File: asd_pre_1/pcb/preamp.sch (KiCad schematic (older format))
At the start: 0 parts

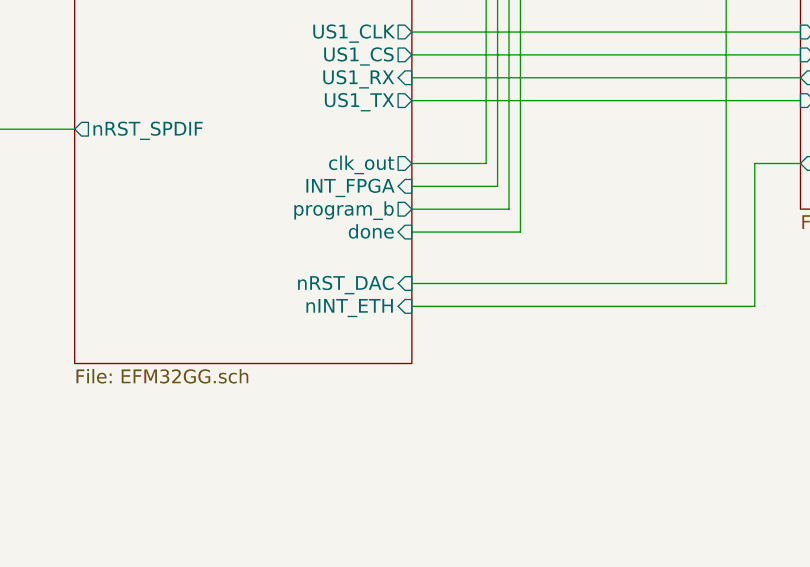
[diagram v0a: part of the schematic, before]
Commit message: Updated schematics and PCB.  Removed some minor errors with the first prototype.
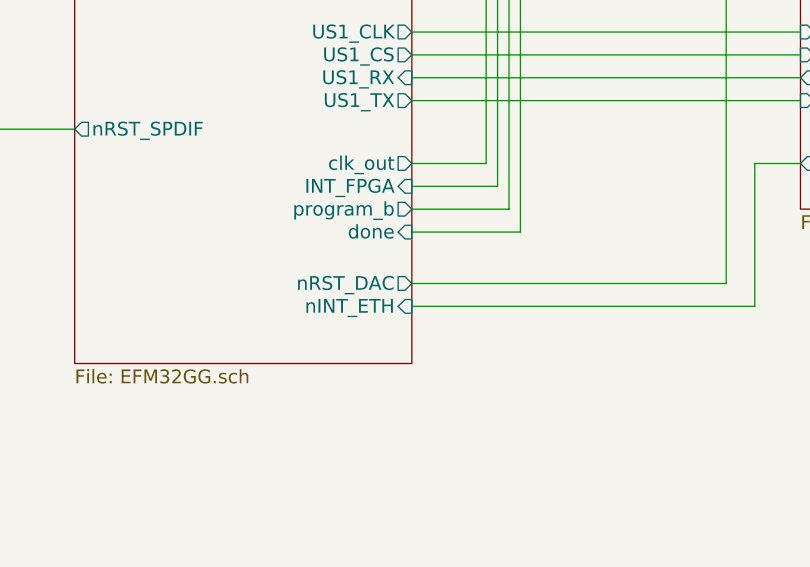
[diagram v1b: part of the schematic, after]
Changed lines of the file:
@@
 EESchema Schematic File Version 2
+LIBS:preamp-rescue
 LIBS:power
 LIBS:device
@@
 LIBS:memory
 LIBS:xilinx
-LIBS:special
 LIBS:microcontrollers
 LIBS:dsp
@@
 encoding utf-8
 Sheet 1 9
-Title ""
+Title "AsD Pre 1 Digital Preamplifier"
 Date ""
 Rev ""
-Comp ""
+Comp "Asbjørn Djupdal"
 Comment1 ""
 Comment2 ""
@@
 F14 "program_b" O R 6700 5675 60
 F15 "done" I R 6700 5775 60
-F16 "nRST_DAC" I R 6700 6000 60
+F16 "nRST_DAC" O R 6700 6000 60
 F17 "nINT_ETH" I R 6700 6100 60
 F18 "nRST_ADC" O L 5225 4500 60
